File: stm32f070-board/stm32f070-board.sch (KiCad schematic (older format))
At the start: 37 parts

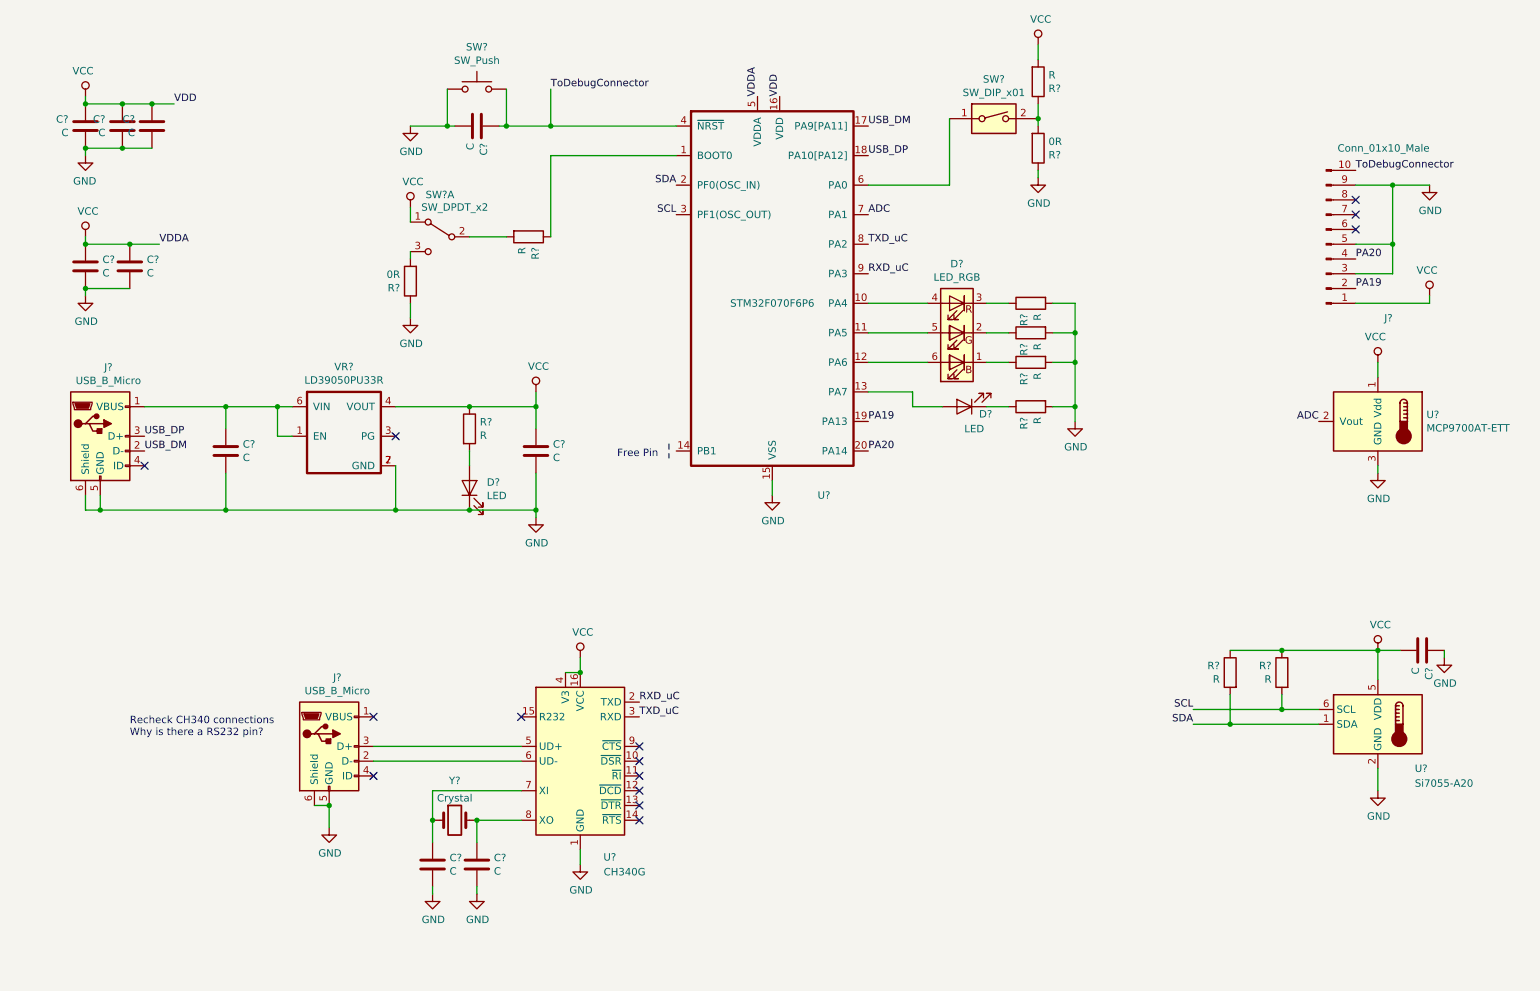
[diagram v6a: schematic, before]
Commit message: added values to the components
Signed-off-by: suyash <in.suyash@gmail.com>
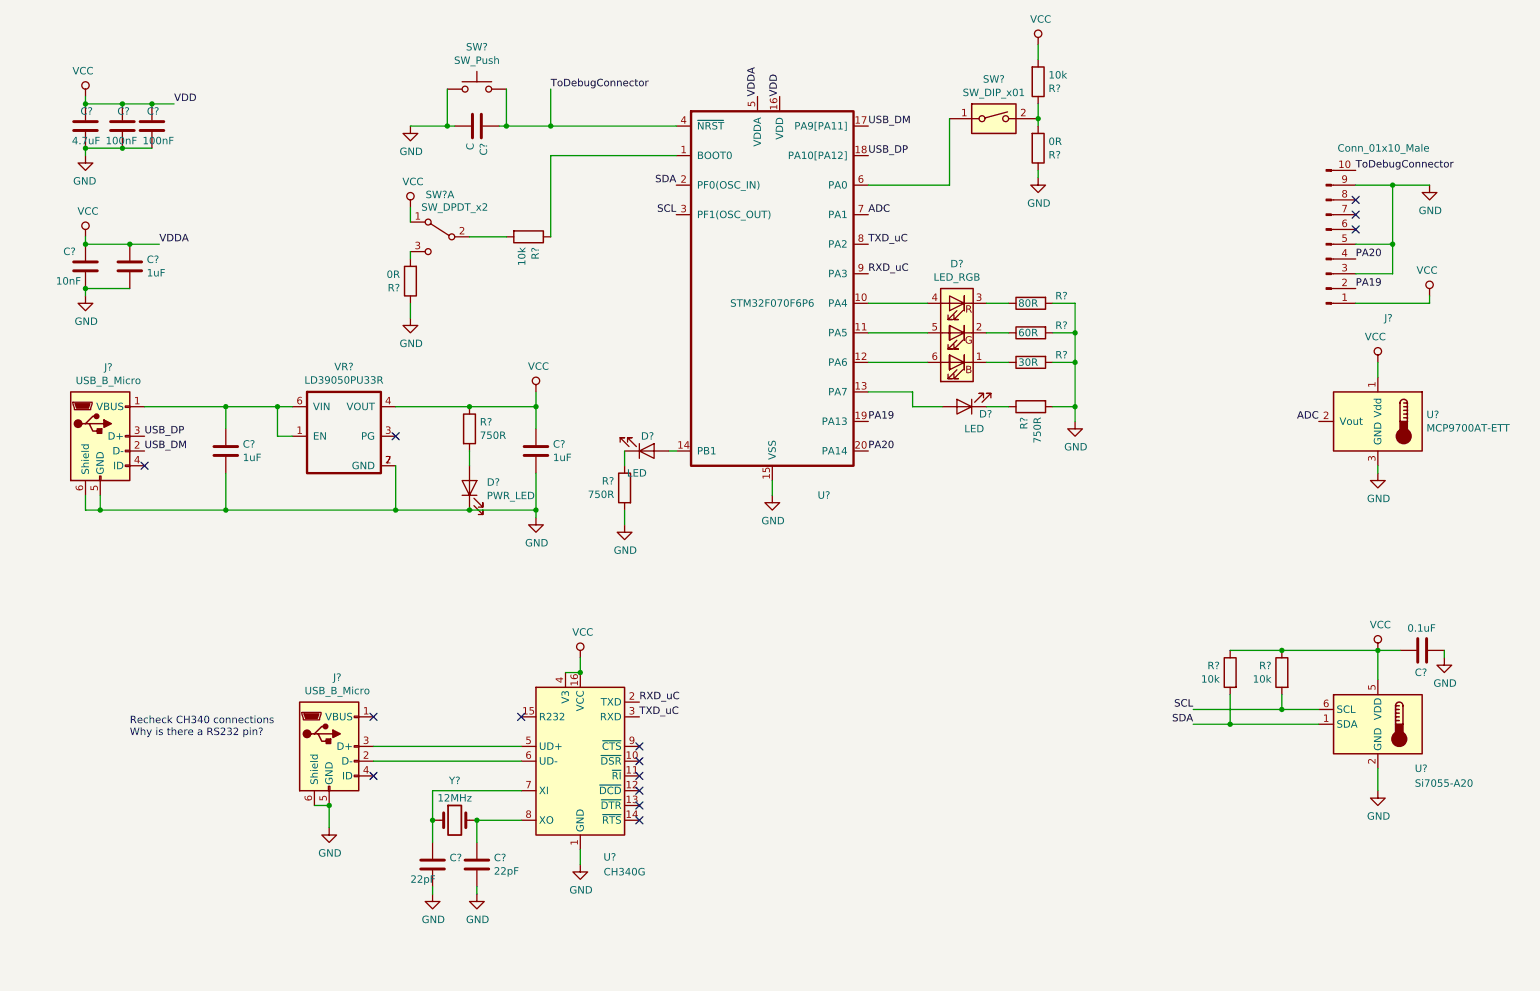
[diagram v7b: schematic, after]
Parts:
- added D?: LED, symbol Device:LED
- added R?: 750R, symbol Device:R
- C? (x3): value C -> 1uF
- C?: value C -> 4.7uF
- C? (x2): value C -> 100nF
- C?: value C -> 10nF
- C?: value C -> 0.1uF
- C? (x2): value C -> 22pF
- D?: value LED -> PWR_LED
- R? (x2): value R -> 750R
- R? (x4): value R -> 10k
- R?: value R -> 30R
- R?: value R -> 60R
- R?: value R -> 80R
- Y?: value Crystal -> 12MHz
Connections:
- net GND: now also R?.2
- net at U?.14 (PB1): now also D?.2 (A)
- new net: D?.1 (K), R?.1
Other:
- note removed: "Free Pin\n"
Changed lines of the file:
@@
 P 2150 3550
 F 0 "C?" H 2265 3596 50  0000 L CNN
-F 1 "C" H 2265 3505 50  0000 L CNN
+F 1 "1uF" H 2265 3505 50  0000 L CNN
 F 2 "" H 2188 3400 50  0001 C CNN
 F 3 "~" H 2150 3550 50  0001 C CNN
@@
 P 3800 3400
 F 0 "R?" H 3870 3446 50  0000 L CNN
-F 1 "R" H 3870 3355 50  0000 L CNN
+F 1 "750R" H 3870 3355 50  0000 L CNN
 F 2 "" V 3730 3400 50  0001 C CNN
 F 3 "~" H 3800 3400 50  0001 C CNN
@@
 P 3800 3800
 F 0 "D?" V 3838 3683 50  0000 R CNN
-F 1 "LED" V 3747 3683 50  0000 R CNN
+F 1 "PWR_LED" V 3747 3683 50  0000 R CNN
 F 2 "" H 3800 3800 50  0001 C CNN
 F 3 "~" H 3800 3800 50  0001 C CNN
@@
 P 4250 3550
 F 0 "C?" H 4365 3596 50  0000 L CNN
-F 1 "C" H 4365 3505 50  0000 L CNN
+F 1 "1uF" H 4365 3505 50  0000 L CNN
 F 2 "" H 4288 3400 50  0001 C CNN
 F 3 "~" H 4250 3550 50  0001 C CNN
@@
 P 4200 2100
 F 0 "R?" H 4270 2146 50  0000 L CNN
-F 1 "R" H 4270 2055 50  0000 L CNN
+F 1 "10k" H 4270 2055 50  0000 L CNN
 F 2 "" V 4130 2100 50  0001 C CNN
 F 3 "~" H 4200 2100 50  0001 C CNN
@@
 U 1 1 5D7AE4EA
 P 1200 1350
-F 0 "C?" H 1315 1396 50  0000 L CNN
-F 1 "C" H 1315 1305 50  0000 L CNN
+F 0 "C?" H 1150 1450 50  0000 L CNN
+F 1 "4.7uF" H 1100 1250 50  0000 L CNN
 F 2 "" H 1238 1200 50  0001 C CNN
 F 3 "~" H 1200 1350 50  0001 C CNN
@@
 U 1 1 5D7AE5E0
 P 1450 1350
-F 0 "C?" H 1565 1396 50  0000 L CNN
-F 1 "C" H 1565 1305 50  0000 L CNN
+F 0 "C?" H 1400 1450 50  0000 L CNN
+F 1 "100nF" H 1350 1250 50  0000 L CNN
 F 2 "" H 1488 1200 50  0001 C CNN
 F 3 "~" H 1450 1350 50  0001 C CNN
@@
 U 1 1 5D7AE616
 P 1650 1350
-F 0 "C?" H 1765 1396 50  0000 L CNN
-F 1 "C" H 1765 1305 50  0000 L CNN
+F 0 "C?" H 1600 1450 50  0000 L CNN
+F 1 "100nF" H 1500 1250 50  0000 L CNN
 F 2 "" H 1688 1200 50  0001 C CNN
 F 3 "~" H 1650 1350 50  0001 C CNN
@@
 P 1500 2300
 F 0 "C?" H 1615 2346 50  0000 L CNN
-F 1 "C" H 1615 2255 50  0000 L CNN
+F 1 "1uF" H 1615 2255 50  0000 L CNN
 F 2 "" H 1538 2150 50  0001 C CNN
 F 3 "~" H 1500 2300 50  0001 C CNN
@@
 U 1 1 5D7B4ED0
 P 1200 2300
-F 0 "C?" H 1315 2346 50  0000 L CNN
-F 1 "C" H 1315 2255 50  0000 L CNN
+F 0 "C?" H 1050 2400 50  0000 L CNN
+F 1 "10nF" H 1000 2200 50  0000 L CNN
 F 2 "" H 1238 2150 50  0001 C CNN
 F 3 "~" H 1200 2300 50  0001 C CNN
@@
 P 7650 1050
 F 0 "R?" H 7720 1096 50  0000 L CNN
-F 1 "R" H 7720 1005 50  0000 L CNN
+F 1 "10k" H 7720 1005 50  0000 L CNN
 F 2 "" V 7580 1050 50  0001 C CNN
 F 3 "~" H 7650 1050 50  0001 C CNN
@@
 P 7600 3250
 F 0 "R?" H 7670 3296 50  0000 L CNN
-F 1 "R" H 7670 3205 50  0000 L CNN
+F 1 "750R" H 7670 3205 50  0000 L CNN
 F 2 "" V 7530 3250 50  0001 C CNN
 F 3 "~" H 7600 3250 50  0001 C CNN
@@
 U 1 1 5D7D845C
 P 7600 2950
-F 0 "R?" H 7670 2996 50  0000 L CNN
-F 1 "R" H 7670 2905 50  0000 L CNN
+F 0 "R?" V 7550 2700 50  0000 L CNN
+F 1 "30R" V 7600 2900 50  0000 L CNN
 F 2 "" V 7530 2950 50  0001 C CNN
 F 3 "~" H 7600 2950 50  0001 C CNN
@@
 U 1 1 5D7D84B2
 P 7600 2750
-F 0 "R?" H 7670 2796 50  0000 L CNN
-F 1 "R" H 7670 2705 50  0000 L CNN
+F 0 "R?" V 7550 2500 50  0000 L CNN
+F 1 "60R" V 7600 2700 50  0000 L CNN
 F 2 "" V 7530 2750 50  0001 C CNN
 F 3 "~" H 7600 2750 50  0001 C CNN
@@
 U 1 1 5D7D84F8
 P 7600 2550
-F 0 "R?" H 7670 2596 50  0000 L CNN
-F 1 "R" H 7670 2505 50  0000 L CNN
+F 0 "R?" V 7550 2300 50  0000 L CNN
+F 1 "80R" V 7600 2500 50  0000 L CNN
 F 2 "" V 7530 2550 50  0001 C CNN
 F 3 "~" H 7600 2550 50  0001 C CNN
@@
 U 1 1 5D8253F2
 P 10250 4900
-F 0 "C?" H 10365 4946 50  0000 L CNN
-F 1 "C" H 10365 4855 50  0000 L CNN
+F 0 "C?" V 10400 4850 50  0000 L CNN
+F 1 "0.1uF" V 10100 4800 50  0000 L CNN
 F 2 "" H 10288 4750 50  0001 C CNN
 F 3 "~" H 10250 4900 50  0001 C CNN
@@
 P 9300 5050
 F 0 "R?" H 9370 5096 50  0000 L CNN
-F 1 "R" H 9370 5005 50  0000 L CNN
+F 1 "10k" H 9370 5005 50  0000 L CNN
 F 2 "" V 9230 5050 50  0001 C CNN
 F 3 "~" H 9300 5050 50  0001 C CNN
@@
 P 8950 5050
 F 0 "R?" H 9020 5096 50  0000 L CNN
-F 1 "R" H 9020 5005 50  0000 L CNN
+F 1 "10k" H 9020 5005 50  0000 L CNN
 F 2 "" V 8880 5050 50  0001 C CNN
 F 3 "~" H 8950 5050 50  0001 C CNN
@@
 Wire Wire Line
 	9950 5850 9950 5700
-Wire Notes Line
-	5150 3500 5150 3600
-Text Notes 4800 3600 0    50   ~ 0
-Free Pin\n
 $Comp
 L Interface_USB:CH340G U?
@@
 P 3700 6050
 F 0 "Y?" H 3700 6318 50  0000 C CNN
-F 1 "Crystal" H 3700 6200 50  0000 C CNN
+F 1 "12MHz" H 3700 6200 50  0000 C CNN
 F 2 "" H 3700 6050 50  0001 C CNN
 F 3 "~" H 3700 6050 50  0001 C CNN
@@
 P 3550 6350
 F 0 "C?" H 3665 6396 50  0000 L CNN
-F 1 "C" H 3665 6305 50  0000 L CNN
+F 1 "22pF" H 3400 6250 50  0000 L CNN
 F 2 "" H 3588 6200 50  0001 C CNN
 F 3 "~" H 3550 6350 50  0001 C CNN
@@
 P 3850 6350
 F 0 "C?" H 3965 6396 50  0000 L CNN
-F 1 "C" H 3965 6305 50  0000 L CNN
+F 1 "22pF" H 3965 6305 50  0000 L CNN
 F 2 "" H 3888 6200 50  0001 C CNN
 F 3 "~" H 3850 6350 50  0001 C CNN
@@
 Wire Wire Line
 	3400 2250 3400 2200
+$Comp
+L Device:LED D?
+U 1 1 5D7DA43F
+P 5000 3550
+F 0 "D?" H 5050 3450 50  0000 R CNN
+F 1 "LED" H 5000 3700 50  0000 R CNN
+F 2 "" H 5000 3550 50  0001 C CNN
+F 3 "~" H 5000 3550 50  0001 C CNN
+	1    5000 3550
+	1    0    0    1
+$EndComp
+$Comp
+L power:GND #PWR?
+U 1 1 5D7DA785
+P 4850 4050
+F 0 "#PWR?" H 4850 3800 50  0001 C CNN
+F 1 "GND" H 4855 3877 50  0000 C CNN
+F 2 "" H 4850 4050 50  0001 C CNN
+F 3 "" H 4850 4050 50  0001 C CNN
+	1    4850 4050
+	1    0    0    -1
+$EndComp
+$Comp
+L Device:R R?
+U 1 1 5D7E3D28
+P 4850 3800
+F 0 "R?" H 4920 3846 50  0000 L CNN
+F 1 "750R" H 4920 3755 50  0000 L CNN
+F 2 "" V 4780 3800 50  0001 C CNN
+F 3 "~" H 4850 3800 50  0001 C CNN
+	1    4850 3800
+	-1   0    0    -1
+$EndComp
+Wire Wire Line
+	4850 4050 4850 3950
+Wire Wire Line
+	4850 3650 4850 3550
+Wire Wire Line
+	5150 3550 5200 3550
 $EndSCHEMATC

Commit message: added component values to missing components(cap parallel to the reset switch and user leds)
Signed-off-by: suyash <in.suyash@gmail.com>
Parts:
- C?: value C -> 100uF
- D?: value LED -> USR_LED1
- D?: value LED -> USR_LED2
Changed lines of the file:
@@
 P 3850 1350
 F 0 "C?" H 3965 1396 50  0000 L CNN
-F 1 "C" H 3965 1305 50  0000 L CNN
+F 1 "100uF" H 3965 1305 50  0000 L CNN
 F 2 "" H 3888 1200 50  0001 C CNN
 F 3 "~" H 3850 1350 50  0001 C CNN
@@
 P 7150 3250
 F 0 "D?" H 7050 3300 50  0000 R CNN
-F 1 "LED" H 7150 3400 50  0000 R CNN
+F 1 "USR_LED1" H 7300 3400 50  0000 R CNN
 F 2 "" H 7150 3250 50  0001 C CNN
 F 3 "~" H 7150 3250 50  0001 C CNN
@@
 P 5000 3550
 F 0 "D?" H 5050 3450 50  0000 R CNN
-F 1 "LED" H 5000 3700 50  0000 R CNN
+F 1 "USR_LED2" H 5250 3650 50  0000 R CNN
 F 2 "" H 5000 3550 50  0001 C CNN
 F 3 "~" H 5000 3550 50  0001 C CNN
